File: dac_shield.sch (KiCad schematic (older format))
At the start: 26 parts, among them P1 V+, P2 GND, P3 V-, P4 Out, P5 GND, U1 LM741, U2 TCA0372

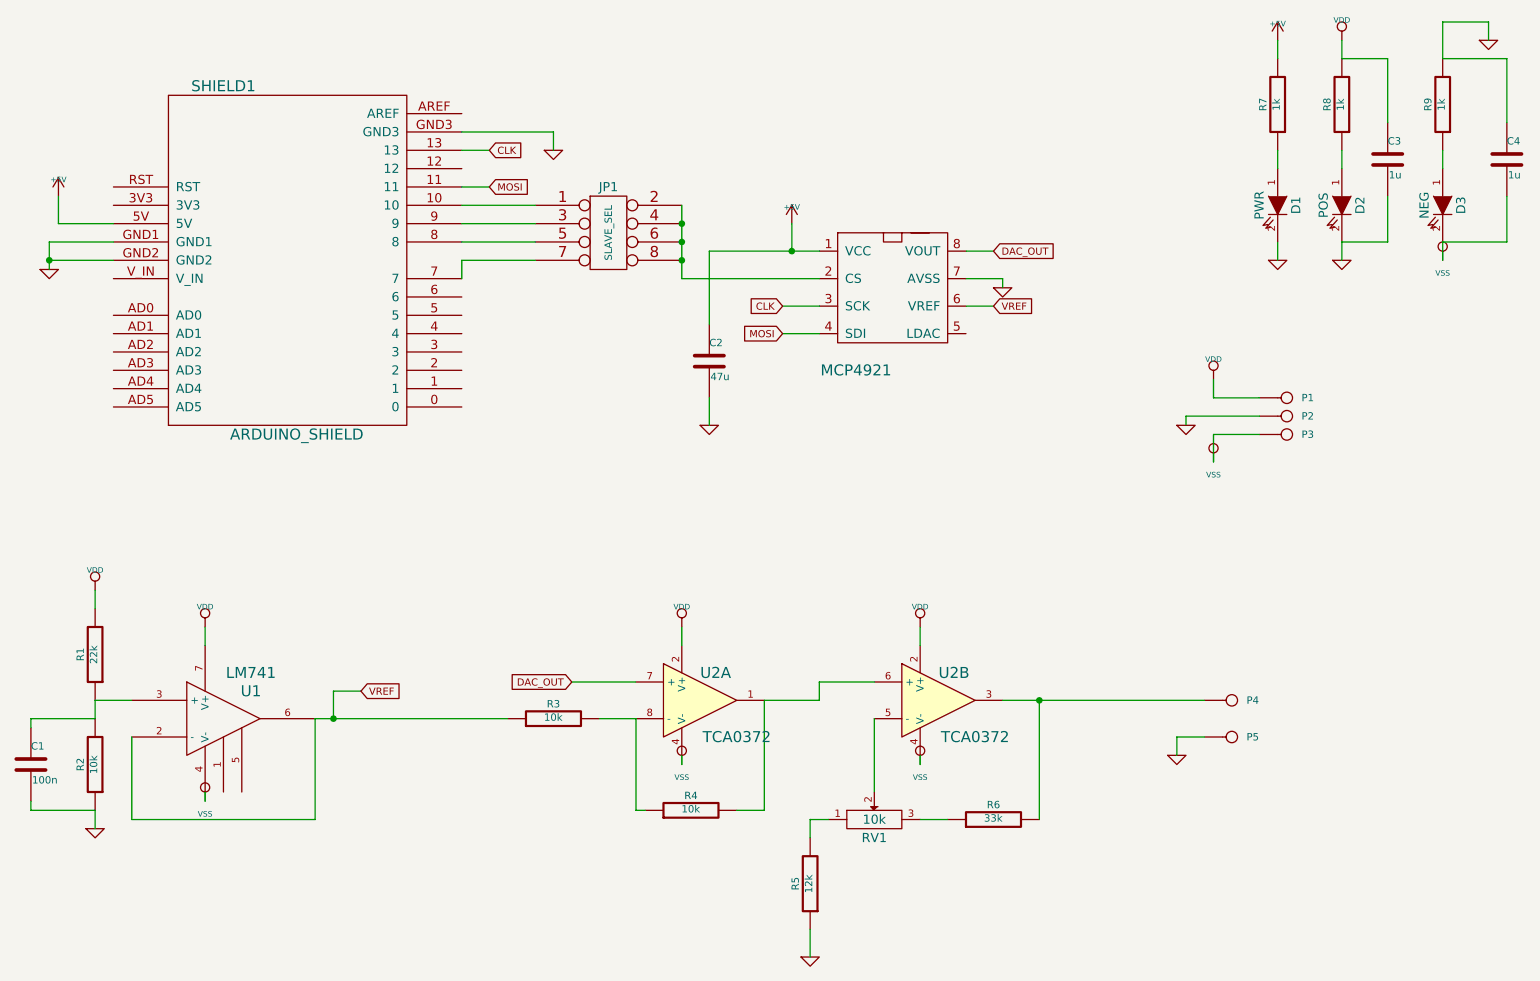
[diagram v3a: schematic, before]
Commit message: Tied LDAC to GND, cleaned up silk screen
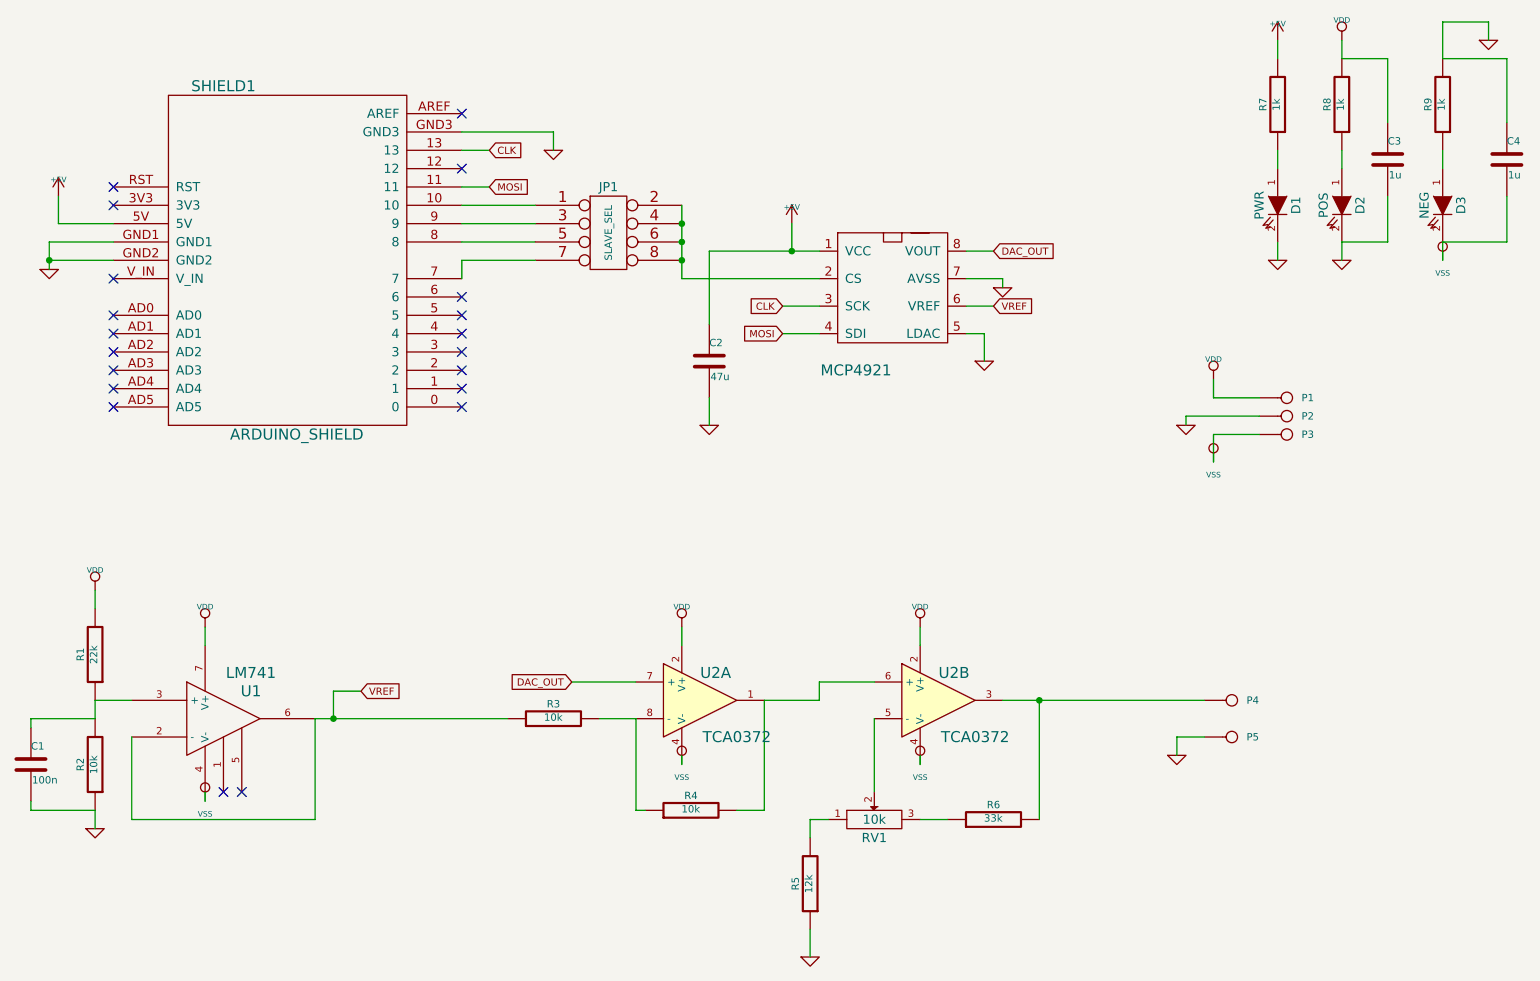
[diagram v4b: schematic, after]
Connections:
- no-connect marks 0 -> 20
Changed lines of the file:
@@
 Sheet 1 1
 Title "Power DAC Shield"
-Date "18 jul 2013"
+Date "23 jul 2013"
 Rev ""
 Comp "Visgence Inc."
@@
 $EndComp
 $Comp
-L MCP4921 #U1
+L MCP4921 #U01
 U 1 1 51E2FDD6
 P 5750 2300
-F 0 "#U1" H 5750 2650 60  0001 C CNN
+F 0 "#U01" H 5750 2650 60  0001 C CNN
 F 1 "MCP4921" H 5550 1850 60  0000 C CNN
 F 2 "" H 5750 2300 60  0000 C CNN
@@
 Connection ~ 4600 1950
 $Comp
-L +5V #PWR2
+L +5V #PWR02
 U 1 1 51E300D3
 P 1200 1800
-F 0 "#PWR2" H 1200 1890 20  0001 C CNN
+F 0 "#PWR02" H 1200 1890 20  0001 C CNN
 F 1 "+5V" H 1200 1890 30  0000 C CNN
 F 2 "" H 1200 1800 60  0000 C CNN
@@
 $EndComp
 $Comp
-L +5V #PWR11
+L +5V #PWR03
 U 1 1 51E300EF
 P 5200 1950
-F 0 "#PWR11" H 5200 2040 20  0001 C CNN
+F 0 "#PWR03" H 5200 2040 20  0001 C CNN
 F 1 "+5V" H 5200 2040 30  0000 C CNN
 F 2 "" H 5200 1950 60  0000 C CNN
@@
 	5200 2100 5200 1950
 $Comp
-L GND #PWR7
+L GND #PWR04
 U 1 1 51E30124
 P 3900 1550
-F 0 "#PWR7" H 3900 1550 30  0001 C CNN
+F 0 "#PWR04" H 3900 1550 30  0001 C CNN
 F 1 "GND" H 3900 1480 30  0001 C CNN
 F 2 "" H 3900 1550 60  0000 C CNN
@@
 	3900 1450 3900 1550
 $Comp
-L GND #PWR1
+L GND #PWR05
 U 1 1 51E3017A
 P 1150 2200
-F 0 "#PWR1" H 1150 2200 30  0001 C CNN
+F 0 "#PWR05" H 1150 2200 30  0001 C CNN
 F 1 "GND" H 1150 2130 30  0001 C CNN
 F 2 "" H 1150 2200 60  0000 C CNN
@@
 $EndComp
 $Comp
-L GND #PWR15
+L GND #PWR06
 U 1 1 51E30180
 P 6350 2300
-F 0 "#PWR15" H 6350 2300 30  0001 C CNN
+F 0 "#PWR06" H 6350 2300 30  0001 C CNN
 F 1 "GND" H 6350 2230 30  0001 C CNN
 F 2 "" H 6350 2300 60  0000 C CNN
@@
 $EndComp
 $Comp
-L VSS #PWR14
+L VSS #PWR07
 U 1 1 51E3066F
 P 5900 4900
-F 0 "#PWR14" H 5900 4900 30  0001 C CNN
+F 0 "#PWR07" H 5900 4900 30  0001 C CNN
 F 1 "VSS" H 5900 4830 30  0000 C CNN
 F 2 "" H 5900 4900 60  0000 C CNN
@@
 $EndComp
 $Comp
-L VDD #PWR13
+L VDD #PWR08
 U 1 1 51E3067E
 P 5900 4150
-F 0 "#PWR13" H 5900 4250 30  0001 C CNN
+F 0 "#PWR08" H 5900 4250 30  0001 C CNN
 F 1 "VDD" H 5900 4260 30  0000 C CNN
 F 2 "" H 5900 4150 60  0000 C CNN
@@
 $EndComp
 $Comp
-L VDD #PWR8
+L VDD #PWR09
 U 1 1 51E3068B
 P 4600 4150
-F 0 "#PWR8" H 4600 4250 30  0001 C CNN
+F 0 "#PWR09" H 4600 4250 30  0001 C CNN
 F 1 "VDD" H 4600 4260 30  0000 C CNN
 F 2 "" H 4600 4150 60  0000 C CNN
@@
 $EndComp
 $Comp
-L VSS #PWR9
+L VSS #PWR010
 U 1 1 51E30691
 P 4600 4900
-F 0 "#PWR9" H 4600 4900 30  0001 C CNN
+F 0 "#PWR010" H 4600 4900 30  0001 C CNN
 F 1 "VSS" H 4600 4830 30  0000 C CNN
 F 2 "" H 4600 4900 60  0000 C CNN
@@
 	5300 5200 5400 5200
 $Comp
-L GND #PWR12
+L GND #PWR011
 U 1 1 51E307ED
 P 5300 5950
-F 0 "#PWR12" H 5300 5950 30  0001 C CNN
+F 0 "#PWR011" H 5300 5950 30  0001 C CNN
 F 1 "GND" H 5300 5880 30  0001 C CNN
 F 2 "" H 5300 5950 60  0000 C CNN
@@
 	1600 5200 1600 4750
 $Comp
-L VSS #PWR6
+L VSS #PWR012
 U 1 1 51E30A90
 P 2000 5100
-F 0 "#PWR6" H 2000 5100 30  0001 C CNN
+F 0 "#PWR012" H 2000 5100 30  0001 C CNN
 F 1 "VSS" H 2000 5030 30  0000 C CNN
 F 2 "" H 2000 5100 60  0000 C CNN
@@
 	2000 5050 2000 5100
 $Comp
-L VDD #PWR5
+L VDD #PWR013
 U 1 1 51E30AC8
 P 2000 4150
-F 0 "#PWR5" H 2000 4250 30  0001 C CNN
+F 0 "#PWR013" H 2000 4250 30  0001 C CNN
 F 1 "VDD" H 2000 4260 30  0000 C CNN
 F 2 "" H 2000 4150 60  0000 C CNN
@@
 $EndComp
 $Comp
-L VDD #PWR3
+L VDD #PWR014
 U 1 1 51E30B13
 P 1400 3950
-F 0 "#PWR3" H 1400 4050 30  0001 C CNN
+F 0 "#PWR014" H 1400 4050 30  0001 C CNN
 F 1 "VDD" H 1400 4060 30  0000 C CNN
 F 2 "" H 1400 3950 60  0000 C CNN
@@
 $EndComp
 $Comp
-L GND #PWR4
+L GND #PWR015
 U 1 1 51E30B25
 P 1400 5250
-F 0 "#PWR4" H 1400 5250 30  0001 C CNN
+F 0 "#PWR015" H 1400 5250 30  0001 C CNN
 F 1 "GND" H 1400 5180 30  0001 C CNN
 F 2 "" H 1400 5250 60  0000 C CNN
@@
 	1200 1950 1200 1800
 $Comp
-L VDD #PWR18
+L VDD #PWR016
 U 1 1 51E30D84
 P 7500 2800
-F 0 "#PWR18" H 7500 2900 30  0001 C CNN
+F 0 "#PWR016" H 7500 2900 30  0001 C CNN
 F 1 "VDD" H 7500 2910 30  0000 C CNN
 F 2 "" H 7500 2800 60  0000 C CNN
@@
 	7500 2900 7500 2800
 $Comp
-L VSS #PWR19
+L VSS #PWR017
 U 1 1 51E30DC8
 P 7500 3250
-F 0 "#PWR19" H 7500 3250 30  0001 C CNN
+F 0 "#PWR017" H 7500 3250 30  0001 C CNN
 F 1 "VSS" H 7500 3180 30  0000 C CNN
 F 2 "" H 7500 3250 60  0000 C CNN
@@
 	7500 3100 7500 3250
 $Comp
-L GND #PWR17
+L GND #PWR018
 U 1 1 51E30E0E
 P 7350 3050
-F 0 "#PWR17" H 7350 3050 30  0001 C CNN
+F 0 "#PWR018" H 7350 3050 30  0001 C CNN
 F 1 "GND" H 7350 2980 30  0001 C CNN
 F 2 "" H 7350 3050 60  0000 C CNN
@@
 Connection ~ 6550 4550
 $Comp
-L GND #PWR16
+L GND #PWR019
 U 1 1 51E30EF3
 P 7300 4850
-F 0 "#PWR16" H 7300 4850 30  0001 C CNN
+F 0 "#PWR019" H 7300 4850 30  0001 C CNN
 F 1 "GND" H 7300 4780 30  0001 C CNN
 F 2 "" H 7300 4850 60  0000 C CNN
@@
 Connection ~ 5200 2100
 $Comp
-L GND #PWR10
+L GND #PWR020
 U 1 1 51E82617
 P 4750 3050
-F 0 "#PWR10" H 4750 3050 30  0001 C CNN
+F 0 "#PWR020" H 4750 3050 30  0001 C CNN
 F 1 "GND" H 4750 2980 30  0001 C CNN
 F 2 "" H 4750 3050 60  0000 C CNN
@@
 	4750 2900 4750 3050
 $Comp
-L +5V #PWR20
+L +5V #PWR021
 U 1 1 51E8266A
 P 7850 950
-F 0 "#PWR20" H 7850 1040 20  0001 C CNN
+F 0 "#PWR021" H 7850 1040 20  0001 C CNN
 F 1 "+5V" H 7850 1040 30  0000 C CNN
 F 2 "" H 7850 950 60  0000 C CNN
@@
 $EndComp
 $Comp
-L GND #PWR21
+L GND #PWR022
 U 1 1 51E8267F
 P 7850 2150
-F 0 "#PWR21" H 7850 2150 30  0001 C CNN
+F 0 "#PWR022" H 7850 2150 30  0001 C CNN
 F 1 "GND" H 7850 2080 30  0001 C CNN
 F 2 "" H 7850 2150 60  0000 C CNN
@@
 	7850 950  7850 1050
 $Comp
-L VDD #PWR22
+L VDD #PWR023
 U 1 1 51E827A2
 P 8200 950
-F 0 "#PWR22" H 8200 1050 30  0001 C CNN
+F 0 "#PWR023" H 8200 1050 30  0001 C CNN
 F 1 "VDD" H 8200 1060 30  0000 C CNN
 F 2 "" H 8200 950 60  0000 C CNN
@@
 	8200 1550 8200 1650
 $Comp
-L GND #PWR23
+L GND #PWR024
 U 1 1 51E82857
 P 8200 2150
-F 0 "#PWR23" H 8200 2150 30  0001 C CNN
+F 0 "#PWR024" H 8200 2150 30  0001 C CNN
 F 1 "GND" H 8200 2080 30  0001 C CNN
 F 2 "" H 8200 2150 60  0000 C CNN
@@
 	8200 2050 8200 2150
 $Comp
-L GND #PWR25
+L GND #PWR025
 U 1 1 51E828BA
 P 9000 950
-F 0 "#PWR25" H 9000 950 30  0001 C CNN
+F 0 "#PWR025" H 9000 950 30  0001 C CNN
 F 1 "GND" H 9000 880 30  0001 C CNN
 F 2 "" H 9000 950 60  0000 C CNN
@@
 	8750 1550 8750 1650
 $Comp
-L VSS #PWR24
+L VSS #PWR026
 U 1 1 51E829CC
 P 8750 2150
-F 0 "#PWR24" H 8750 2150 30  0001 C CNN
+F 0 "#PWR026" H 8750 2150 30  0001 C CNN
 F 1 "VSS" H 8750 2080 30  0000 C CNN
 F 2 "" H 8750 2150 60  0000 C CNN
@@
 	1    0    0    -1
 $EndComp
+$Comp
+L GND #PWR027
+U 1 1 51EEC648
+P 6250 2700
+F 0 "#PWR027" H 6250 2700 30  0001 C CNN
+F 1 "GND" H 6250 2630 30  0001 C CNN
+F 2 "" H 6250 2700 60  0000 C CNN
+F 3 "" H 6250 2700 60  0000 C CNN
+	1    6250 2700
+	1    0    0    -1
+$EndComp
+Wire Wire Line
+	6150 2550 6250 2550
+Wire Wire Line
+	6250 2550 6250 2700
+NoConn ~ 1500 1750
+NoConn ~ 1500 1850
+NoConn ~ 1500 2250
+NoConn ~ 1500 2450
+NoConn ~ 1500 2550
+NoConn ~ 1500 2650
+NoConn ~ 1500 2750
+NoConn ~ 1500 2850
+NoConn ~ 1500 2950
+NoConn ~ 3400 2950
+NoConn ~ 3400 2850
+NoConn ~ 3400 2750
+NoConn ~ 3400 2650
+NoConn ~ 3400 2550
+NoConn ~ 3400 2450
+NoConn ~ 3400 2350
+NoConn ~ 3400 1650
+NoConn ~ 3400 1350
+NoConn ~ 2100 5050
+NoConn ~ 2200 5050
 $EndSCHEMATC
